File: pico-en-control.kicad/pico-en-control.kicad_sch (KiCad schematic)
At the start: 17 parts, among them J1 JST-PH2 Bat, J2 Pico Pin 1-7, J3 Pico Pin 40-34, SW1 SW_Push, U1 SN74HC74N, U2 PCF8563T, Y1 Crystal

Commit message: draft routing
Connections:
- net +3V3: now also R5.2
- net +BATT: no longer R5.1
- net CLKOUT: now also R5.1; no longer R5.2
- net GP5_DONE: now reaches J2.7 (Pin_7)
- net GP5_DONE: now also R1.2, U1.3 (1CLK)
- net GP2: no longer names the net of J2.2 (Pin_2)
- net GP2: no longer JP1.1 (A)
- removed net GP4_DONE: J2.6 (Pin_6), R1.2, U1.3 (1CLK)
- new net GP4_CLKOUT: J2.6 (Pin_6), JP1.1 (A)
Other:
- moved on the sheet: R5

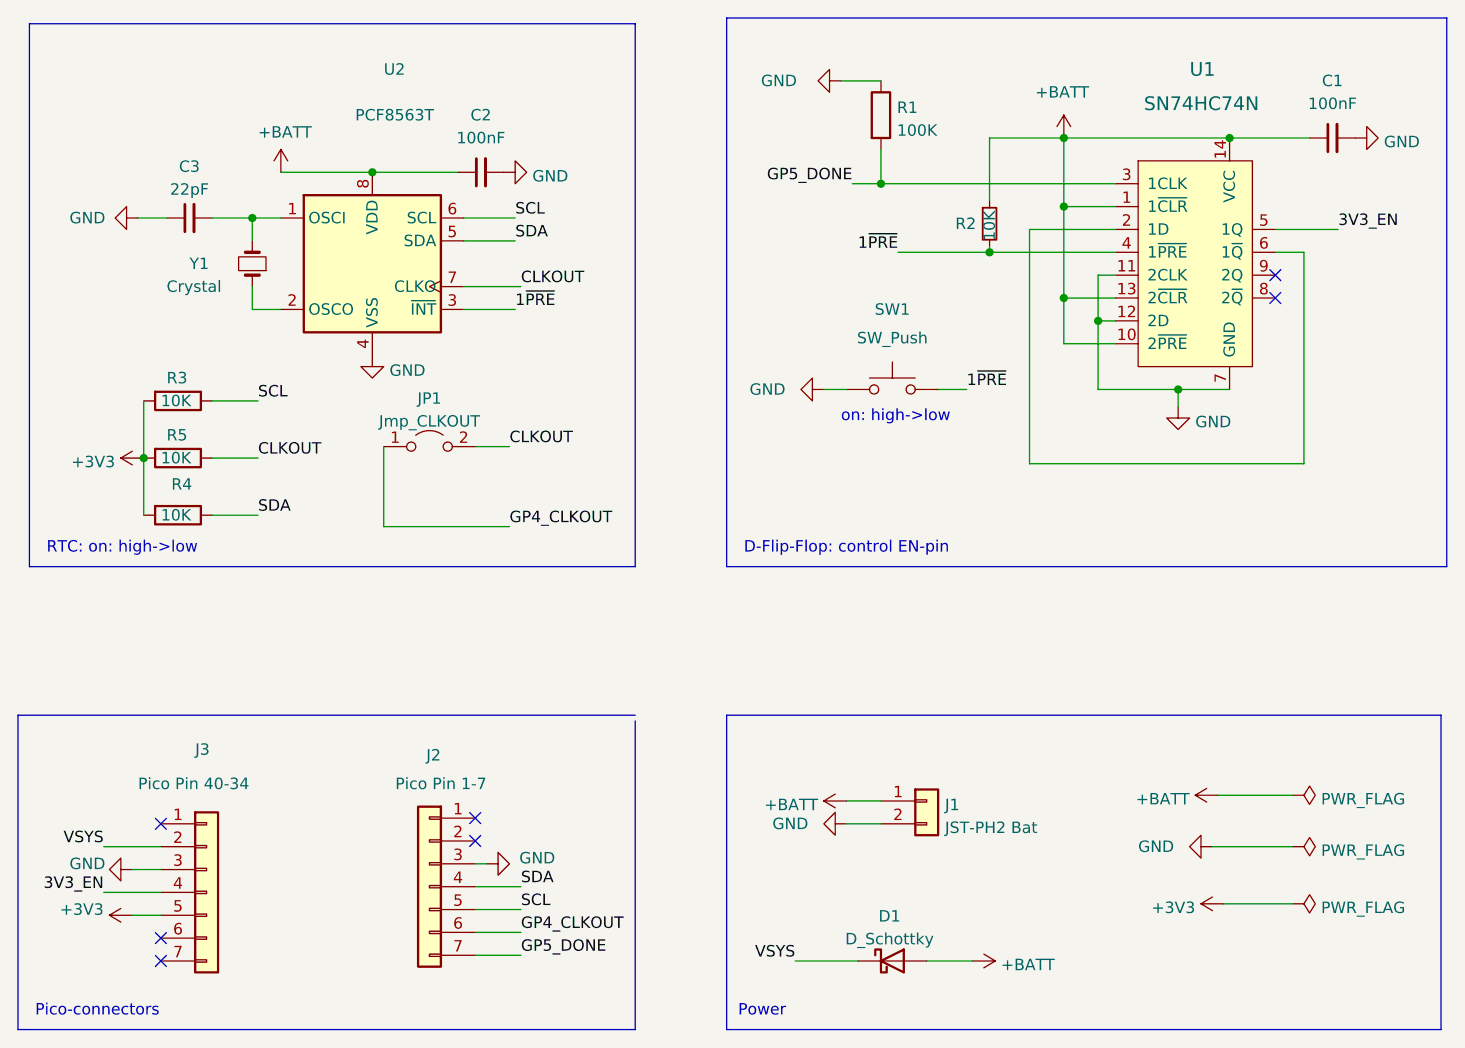
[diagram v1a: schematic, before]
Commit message: switched to 13-pin connectors
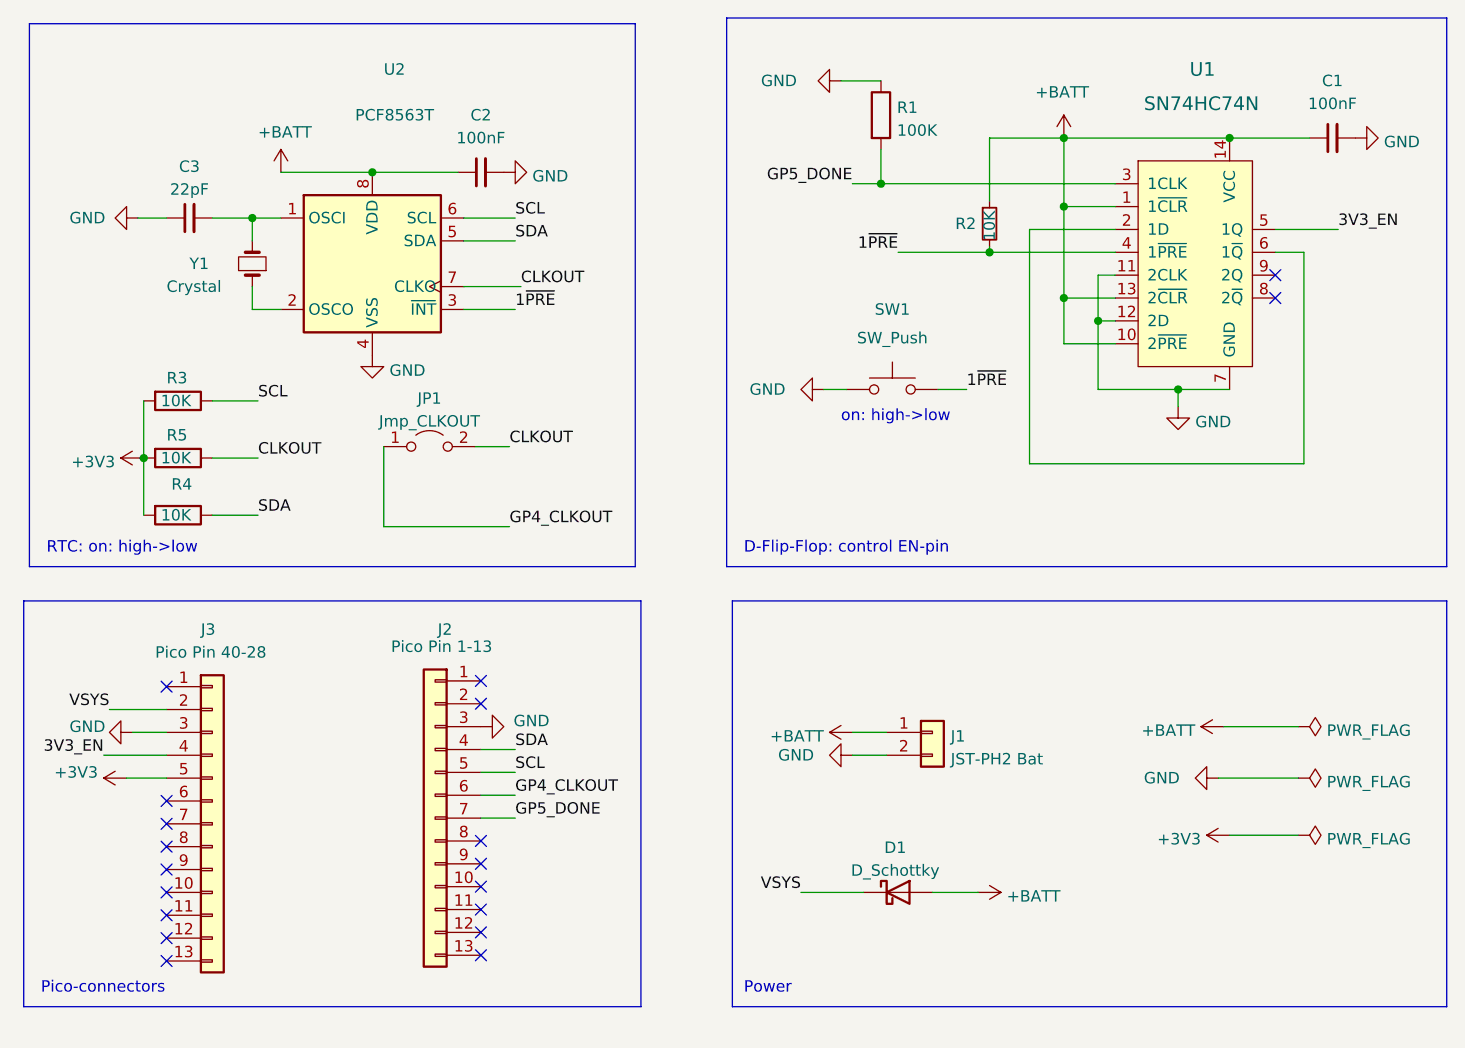
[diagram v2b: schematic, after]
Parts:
- J2: value Pico Pin 1-7 -> Pico Pin 1-13; footprint user:Connector_1x7_no_solder -> user:Connector_1x13_no_solder; symbol Connector_Generic:Conn_01x07 -> Connector_Generic:Conn_01x13
- J3: value Pico Pin 40-34 -> Pico Pin 40-28; footprint user:Connector_1x7_no_solder -> user:Connector_1x13_no_solder; symbol Connector_Generic:Conn_01x07 -> Connector_Generic:Conn_01x13
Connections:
- no-connect marks 7 -> 19
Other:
- moved on the sheet: D1, J1

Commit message: DRC ok
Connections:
- net GND: now also J2.13 (Pin_13), J2.8 (Pin_8), J3.13 (Pin_13), J3.8 (Pin_8)
- no-connect marks 19 -> 15
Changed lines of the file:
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@@
   )
   (no_connect (at 88.9 128.27))
-  (no_connect (at 88.9 125.73))
   (no_connect (at 123.825 130.175))
   (no_connect (at 123.825 107.315))
   (no_connect (at 123.825 109.855))
-  (no_connect (at 88.9 138.43))
   (no_connect (at 123.825 127.635))
   (no_connect (at 88.9 133.35))
   (no_connect (at 123.825 132.715))
-  (no_connect (at 123.825 125.095))
-  (no_connect (at 123.825 137.795))
   (no_connect (at 88.9 135.89))
   (no_connect (at 88.9 120.65))
@@
     (stroke (width 0) (type default) (color 0 0 0 0))
   )
+  (wire (pts (xy 85.09 138.43) (xy 88.9 138.43))
+    (stroke (width 0) (type default) (color 0 0 0 0))
+  )
   (polyline (pts (xy 151.13 33.655) (xy 151.13 94.615))
     (stroke (width 0) (type default) (color 0 0 0 0))
@@
   )
   (polyline (pts (xy 73.66 34.29) (xy 73.66 94.615))
+    (stroke (width 0) (type default) (color 0 0 0 0))
+  )
+  (wire (pts (xy 85.09 125.73) (xy 88.9 125.73))
     (stroke (width 0) (type default) (color 0 0 0 0))
   )
@@
     (pin "2")
   )
+  (symbol (lib_id "power:GND") (at 123.825 137.795 90) (mirror x) (unit 1)
+    (in_bom yes) (on_board yes)
+    (property "Reference" "#PWR?" (id 0) (at 130.175 137.795 0)
+      (effects (font (size 1.27 1.27)) hide)
+    )
+    (property "Value" "GND" (id 1) (at 131.445 137.16 90)
+      (effects (font (size 1.27 1.27)) (justify left))
+    )
+    (property "Footprint" "" (id 2) (at 123.825 137.795 0)
+      (effects (font (size 1.27 1.27)) hide)
+    )
+    (property "Datasheet" "" (id 3) (at 123.825 137.795 0)
+      (effects (font (size 1.27 1.27)) hide)
+    )
+    (pin "1")
+  )
   (symbol (lib_id "power:+3V3") (at 86.36 82.55 90) (unit 1)
     (in_bom yes) (on_board yes) (fields_autoplaced)
@@
     )
     (property "Datasheet" "" (id 3) (at 161.925 74.93 0)
+      (effects (font (size 1.27 1.27)) hide)
+    )
+    (pin "1")
+  )
+  (symbol (lib_id "power:GND") (at 85.09 138.43 270) (unit 1)
+    (in_bom yes) (on_board yes)
+    (property "Reference" "#PWR?" (id 0) (at 78.74 138.43 0)
+      (effects (font (size 1.27 1.27)) hide)
+    )
+    (property "Value" "GND" (id 1) (at 78.105 137.795 90)
+      (effects (font (size 1.27 1.27)) (justify left))
+    )
+    (property "Footprint" "" (id 2) (at 85.09 138.43 0)
+      (effects (font (size 1.27 1.27)) hide)
+    )
+    (property "Datasheet" "" (id 3) (at 85.09 138.43 0)
       (effects (font (size 1.27 1.27)) hide)
     )
@@
     (pin "1")
   )
+  (symbol (lib_id "power:GND") (at 85.09 125.73 270) (unit 1)
+    (in_bom yes) (on_board yes)
+    (property "Reference" "#PWR?" (id 0) (at 78.74 125.73 0)
+      (effects (font (size 1.27 1.27)) hide)
+    )
+    (property "Value" "GND" (id 1) (at 78.105 125.095 90)
+      (effects (font (size 1.27 1.27)) (justify left))
+    )
+    (property "Footprint" "" (id 2) (at 85.09 125.73 0)
+      (effects (font (size 1.27 1.27)) hide)
+    )
+    (property "Datasheet" "" (id 3) (at 85.09 125.73 0)
+      (effects (font (size 1.27 1.27)) hide)
+    )
+    (pin "1")
+  )
   (symbol (lib_id "power:+BATT") (at 165.1 113.03 90) (unit 1)
     (in_bom yes) (on_board yes) (fields_autoplaced)
@@
     (pin "1")
   )
+  (symbol (lib_id "power:GND") (at 123.825 125.095 90) (mirror x) (unit 1)
+    (in_bom yes) (on_board yes)
+    (property "Reference" "#PWR?" (id 0) (at 130.175 125.095 0)
+      (effects (font (size 1.27 1.27)) hide)
+    )
+    (property "Value" "GND" (id 1) (at 131.445 124.46 90)
+      (effects (font (size 1.27 1.27)) (justify left))
+    )
+    (property "Footprint" "" (id 2) (at 123.825 125.095 0)
+      (effects (font (size 1.27 1.27)) hide)
+    )
+    (property "Datasheet" "" (id 3) (at 123.825 125.095 0)
+      (effects (font (size 1.27 1.27)) hide)
+    )
+    (pin "1")
+  )
   (symbol (lib_id "power:GND") (at 220.98 46.99 90) (unit 1)
     (in_bom yes) (on_board yes) (fields_autoplaced)
@@
       (reference "#PWR0105") (unit 1) (value "+3V3") (footprint "")
     )
+    (path "/2721609c-f161-4649-8caf-b27c7748cbdb"
+      (reference "#PWR?") (unit 1) (value "GND") (footprint "")
+    )
+    (path "/3e266c6d-5aba-467c-9ae1-a13ae4e195a5"
+      (reference "#PWR?") (unit 1) (value "GND") (footprint "")
+    )
+    (path "/9daade84-f146-4e38-9889-9c3ac72475f9"
+      (reference "#PWR?") (unit 1) (value "GND") (footprint "")
+    )
+    (path "/da0d7de8-a385-4e20-96bb-738a9abcf740"
+      (reference "#PWR?") (unit 1) (value "GND") (footprint "")
+    )
     (path "/5bee97ec-80e1-4be7-a685-5921db869610"

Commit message: Rev2
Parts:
- removed SW1: SW_Push, user:SW_PUSH_SLIM_1x4, symbol Switch:SW_Push
- added SW1: SW_Push_SLIM, user:SW_PUSH_SLIM_1x4, symbol user:SW_Push_SLIM
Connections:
- net 1~{PRE}: now also SW1.2
- net GND: now also SW1.1, SW1.3 (1)
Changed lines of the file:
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@@
+    (stroke (width 0) (type default) (color 0 0 0 0))
+  )
+  (wire (pts (xy 161.925 77.47) (xy 164.465 77.47))
     (stroke (width 0) (type default) (color 0 0 0 0))
   )
@@
     (effects (font (size 1.27 1.27)) (justify left bottom))
   )
-  (text "on: high->low" (at 163.83 78.74 0)
+  (text "on: high->low" (at 163.195 81.915 0)
     (effects (font (size 1.27 1.27)) (justify left bottom))
   )
@@
   (symbol (lib_id "power:GND") (at 123.825 137.795 90) (mirror x) (unit 1)
     (in_bom yes) (on_board yes)
-    (property "Reference" "#PWR?" (id 0) (at 130.175 137.795 0)
+    (property "Reference" "#PWR0107" (id 0) (at 130.175 137.795 0)
       (effects (font (size 1.27 1.27)) hide)
     )
@@
     (pin "1")
   )
+  (symbol (lib_id "power:GND") (at 161.925 77.47 270) (unit 1)
+    (in_bom yes) (on_board yes)
+    (property "Reference" "#PWR0110" (id 0) (at 155.575 77.47 0)
+      (effects (font (size 1.27 1.27)) hide)
+    )
+    (property "Value" "GND" (id 1) (at 153.67 77.47 90)
+      (effects (font (size 1.27 1.27)) (justify left))
+    )
+    (property "Footprint" "" (id 2) (at 161.925 77.47 0)
+      (effects (font (size 1.27 1.27)) hide)
+    )
+    (property "Datasheet" "" (id 3) (at 161.925 77.47 0)
+      (effects (font (size 1.27 1.27)) hide)
+    )
+    (pin "1")
+  )
   (symbol (lib_id "power:PWR_FLAG") (at 214.63 118.11 270) (unit 1)
     (in_bom yes) (on_board yes) (fields_autoplaced)
@@
   (symbol (lib_id "power:GND") (at 85.09 138.43 270) (unit 1)
     (in_bom yes) (on_board yes)
-    (property "Reference" "#PWR?" (id 0) (at 78.74 138.43 0)
+    (property "Reference" "#PWR0108" (id 0) (at 78.74 138.43 0)
       (effects (font (size 1.27 1.27)) hide)
     )
@@
     (pin "1")
   )
+  (symbol (lib_id "user:SW_Push_SLIM") (at 169.545 74.93 0) (unit 1)
+    (in_bom yes) (on_board yes) (fields_autoplaced)
+    (property "Reference" "SW1" (id 0) (at 169.545 68.3092 0))
+    (property "Value" "SW_Push_SLIM" (id 1) (at 169.545 70.8461 0))
+    (property "Footprint" "user:SW_PUSH_SLIM_1x4" (id 2) (at 169.545 82.55 0)
+      (effects (font (size 1.27 1.27)) hide)
+    )
+    (property "Datasheet" "" (id 3) (at 169.545 69.85 0)
+      (effects (font (size 1.27 1.27)) hide)
+    )
+    (pin "1")
+    (pin "2")
+    (pin "3")
+  )
   (symbol (lib_id "Device:C_Small") (at 218.44 46.99 90) (unit 1)
     (in_bom yes) (on_board yes)
@@
     )
     (property "LCSC" "C25744" (id 4) (at 90.17 82.55 0)
-      (effects (font (size 1.27 1.27)) hide)
-    )
-    (pin "1")
-    (pin "2")
-  )
-  (symbol (lib_id "Switch:SW_Push") (at 169.545 74.93 0) (unit 1)
-    (in_bom yes) (on_board yes)
-    (property "Reference" "SW1" (id 0) (at 169.545 66.04 0))
-    (property "Value" "SW_Push" (id 1) (at 169.545 69.215 0))
-    (property "Footprint" "user:SW_PUSH_SLIM_1x4" (id 2) (at 169.545 69.85 0)
-      (effects (font (size 1.27 1.27)) hide)
-    )
-    (property "Datasheet" "~" (id 3) (at 169.545 69.85 0)
       (effects (font (size 1.27 1.27)) hide)
     )
@@
   (symbol (lib_id "power:GND") (at 85.09 125.73 270) (unit 1)
     (in_bom yes) (on_board yes)
-    (property "Reference" "#PWR?" (id 0) (at 78.74 125.73 0)
+    (property "Reference" "#PWR0109" (id 0) (at 78.74 125.73 0)
       (effects (font (size 1.27 1.27)) hide)
     )
@@
   (symbol (lib_id "power:GND") (at 123.825 125.095 90) (mirror x) (unit 1)
     (in_bom yes) (on_board yes)
-    (property "Reference" "#PWR?" (id 0) (at 130.175 125.095 0)
+    (property "Reference" "#PWR0106" (id 0) (at 130.175 125.095 0)
       (effects (font (size 1.27 1.27)) hide)
     )
@@
       (reference "#PWR0105") (unit 1) (value "+3V3") (footprint "")
     )
+    (path "/da0d7de8-a385-4e20-96bb-738a9abcf740"
+      (reference "#PWR0106") (unit 1) (value "GND") (footprint "")
+    )
     (path "/2721609c-f161-4649-8caf-b27c7748cbdb"
-      (reference "#PWR?") (unit 1) (value "GND") (footprint "")
+      (reference "#PWR0107") (unit 1) (value "GND") (footprint "")
     )
     (path "/3e266c6d-5aba-467c-9ae1-a13ae4e195a5"
-      (reference "#PWR?") (unit 1) (value "GND") (footprint "")
+      (reference "#PWR0108") (unit 1) (value "GND") (footprint "")
     )
     (path "/9daade84-f146-4e38-9889-9c3ac72475f9"
-      (reference "#PWR?") (unit 1) (value "GND") (footprint "")
-    )
-    (path "/da0d7de8-a385-4e20-96bb-738a9abcf740"
-      (reference "#PWR?") (unit 1) (value "GND") (footprint "")
+      (reference "#PWR0109") (unit 1) (value "GND") (footprint "")
+    )
+    (path "/34aa5534-e445-4f46-8589-62223cf8ef18"
+      (reference "#PWR0110") (unit 1) (value "GND") (footprint "")
     )
     (path "/5bee97ec-80e1-4be7-a685-5921db869610"
@@
       (reference "R5") (unit 1) (value "10K") (footprint "Resistor_SMD:R_0402_1005Metric")
     )
-    (path "/8eb4a059-c6b6-4dfe-acee-59cf9f265db1"
-      (reference "SW1") (unit 1) (value "SW_Push") (footprint "user:SW_PUSH_SLIM_1x4")
+    (path "/58a4b577-49cb-4d3a-a75f-433d25045363"
+      (reference "SW1") (unit 1) (value "SW_Push_SLIM") (footprint "user:SW_PUSH_SLIM_1x4")
     )
     (path "/aeee191c-38fd-4ab0-b212-9eafb9d35bdc"
